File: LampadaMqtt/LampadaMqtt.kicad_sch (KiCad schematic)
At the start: 23 parts, among them Q1 BDW93C, U1 ESP32-C3_SUPERMINI_TH, U2 module_bh1750

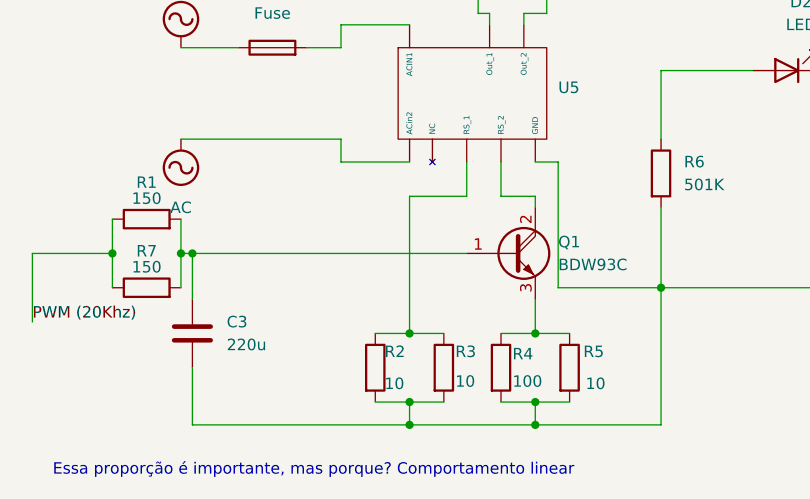
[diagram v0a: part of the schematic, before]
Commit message: Adicionado automations.yaml para refletir automações criadas atualizado esquematica para refletir montagem de fato da lampada e corrigido um erro em mqtt_callback cpp
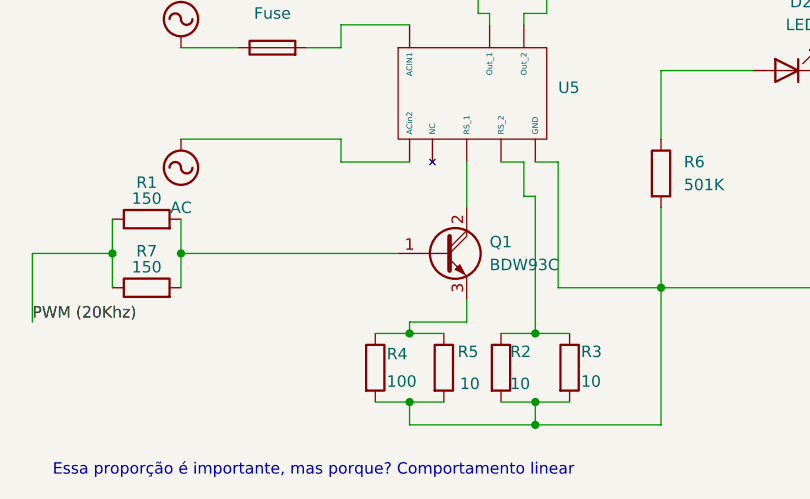
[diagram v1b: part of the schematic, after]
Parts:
- removed C3: 220u, symbol Device:C
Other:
- moved on the sheet: Q1, R2, R3, R4, R5

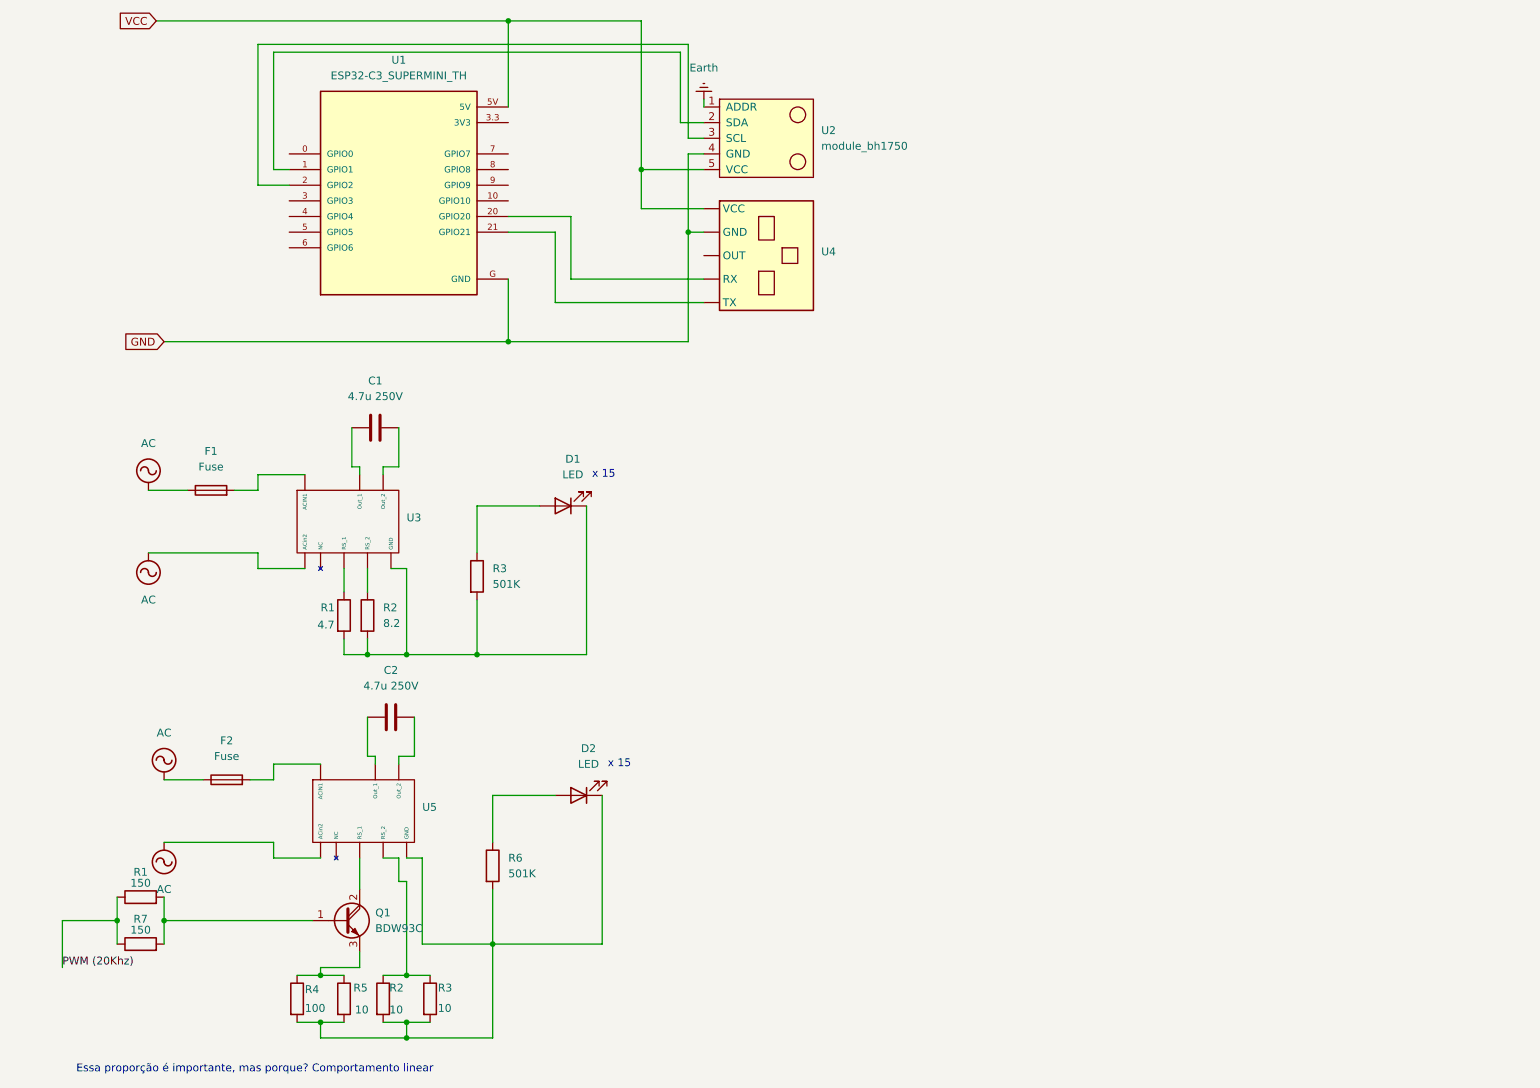
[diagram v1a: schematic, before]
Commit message: Atualização geral para adição de função sleep, relé e controle de brilho
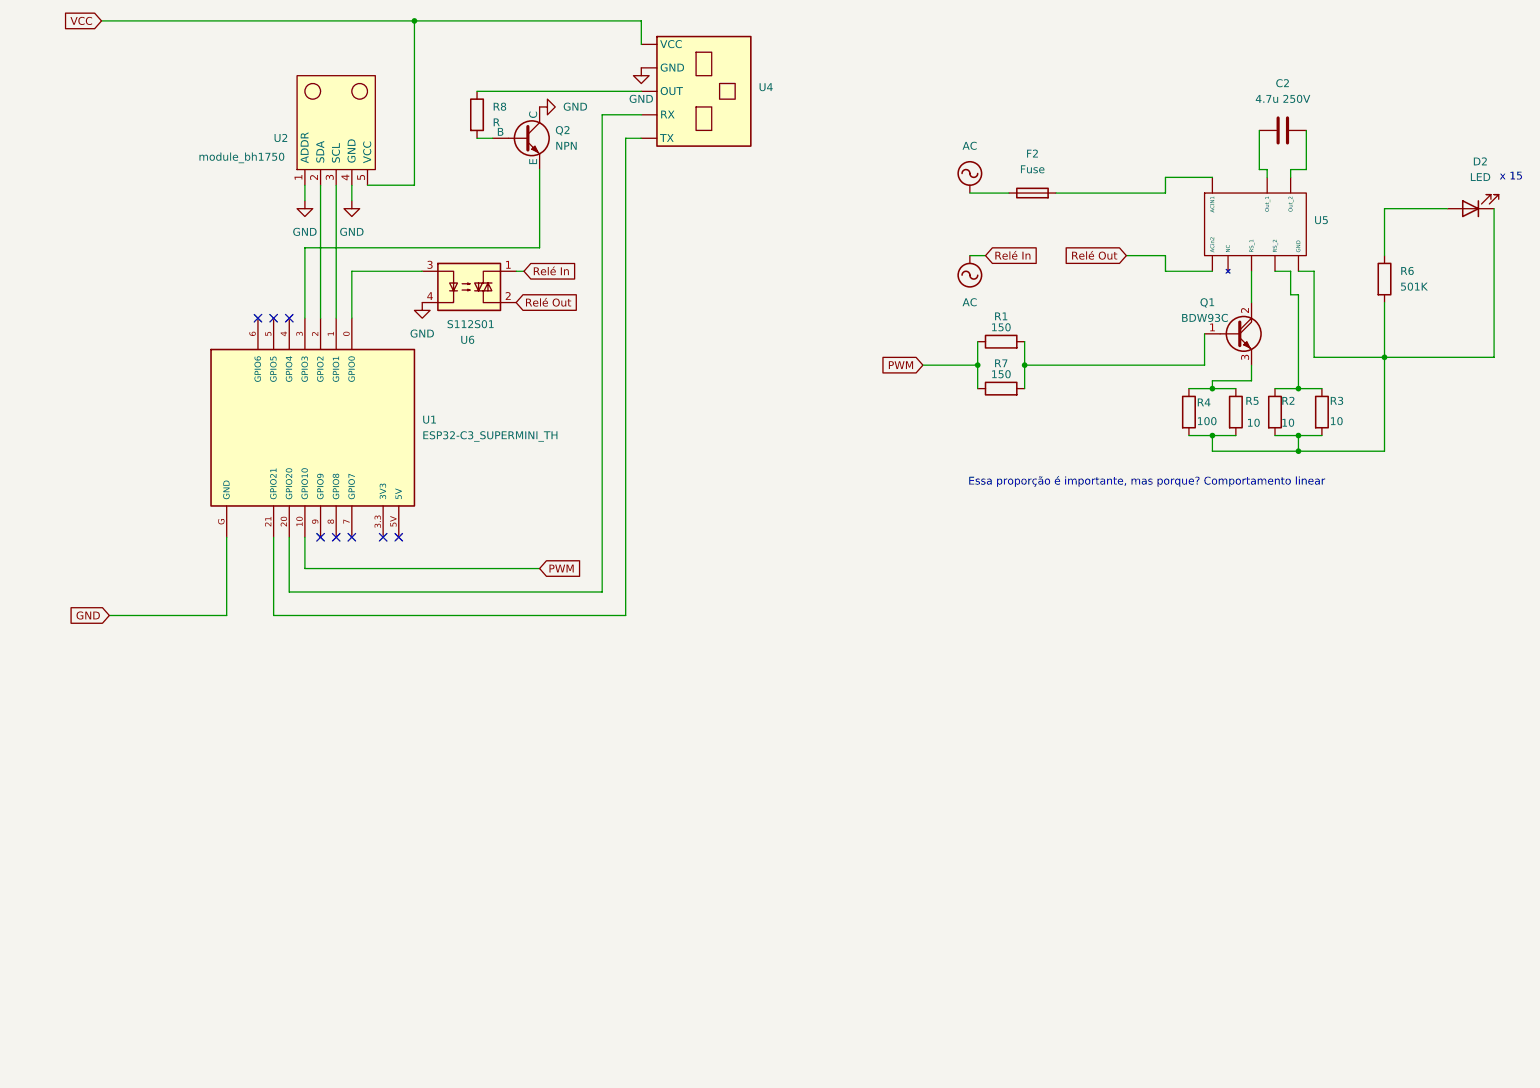
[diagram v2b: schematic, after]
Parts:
- removed C1: 4.7u 250V, symbol Device:C
- removed D1: LED, symbol Device:LED
- removed F1: Fuse, symbol Device:Fuse
- removed R1: 4.7, symbol Device:R
- removed R2: 8.2, symbol Device:R
- removed R3: 501K, symbol Device:R
- removed U3: ~, symbol DIY:JWD1698D
- added Q2: NPN, symbol Simulation_SPICE:NPN
- added R8: R, symbol Device:R
- added U6: S112S01, Package_SIP:SIP4_Sharp-SSR_P7.62mm_Straight, symbol Relay_SolidState:S112S01
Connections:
- net Earth is gone; now on net GND: U2.1 (ADDR)
- net PWM (20Khz) is gone; now on net PWM: R1.1, R7.1
- net AC: now also U6.1; no longer U5. (GND)
- net GND: now also Q2.1 (C), U6.4
- net VCC: no longer U1.5V
- net Relé Out: now reaches U5. (GND)
- net Relé Out: now also U6.2
- net at U2.2 (SDA): now also U1.2 (GPIO2); no longer U1.1 (GPIO1)
- net at U2.3 (SCL): now also U1.1 (GPIO1); no longer U1.2 (GPIO2)
- net at U1.0 (GPIO0): now also U6.3
- net PWM: now reaches U1.10 (GPIO10)
- net at U1.3 (GPIO3): now also Q2.3 (E)
- new net: R8.1, U4. (TX)
- new net: Q2.2 (B), R8.2
- no-connect marks 0 -> 8
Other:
- moved on the sheet: C2, D2, Q1, R1, R2, R3, R4, R5, R6, R7, U1, U2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

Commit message: Adição de sensor de temperatura.
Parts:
- Q2, R8: now not fitted
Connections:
- net VCC: now also U1.5V
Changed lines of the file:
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@@
+	)
+	(no_connect
+		(at 107.95 27.94)
 	)
 	(no_connect
@@
 		(at 66.04 100.33)
 	)
-	(no_connect
-		(at 68.58 100.33)
-	)
 	(wire
 		(pts
@@
 	(wire
 		(pts
+			(xy 68.58 102.87) (xy 66.04 102.87)
+		)
+		(stroke
+			(width 0)
+			(type default)
+		)
+	)
+	(wire
+		(pts
 			(xy 162.56 72.39) (xy 162.56 68.58)
 		)
@@
 		(pts
 			(xy 208.28 34.29) (xy 208.28 40.64)
+		)
+		(stroke
+			(width 0)
+			(type default)
+		)
+	)
+	(wire
+		(pts
+			(xy 68.58 102.87) (xy 68.58 100.33)
 		)
 		(stroke
@@
 				)
 				(justify left)
+				(hide yes)
+			)
+		)
+	)
+	(global_label "VCC"
+		(shape input)
+		(at 66.04 102.87 180)
+		(fields_autoplaced yes)
+		(effects
+			(font
+				(size 1.27 1.27)
+			)
+			(justify right)
+		)
+		(property "Intersheetrefs" "${INTERSHEET_REFS}"
+			(at 59.4262 102.87 0)
+			(effects
+				(font
+					(size 1.27 1.27)
+				)
+				(justify right)
 				(hide yes)
 			)
@@
 		(in_bom yes)
 		(on_board yes)
-		(dnp no)
+		(dnp yes)
 		(fields_autoplaced yes)
 		(property "Reference" "R8"
@@
 		(in_bom yes)
 		(on_board yes)
-		(dnp no)
+		(dnp yes)
 		(fields_autoplaced yes)
 		(property "Reference" "Q2"
@@
 		(on_board yes)
 		(dnp no)
-		(fields_autoplaced yes)
 		(property "Reference" "#PWR06"
 			(at 107.95 30.48 0)
@@
 		)
 		(property "Value" "GND"
-			(at 107.95 29.21 0)
-			(effects
-				(font
+			(at 105.156 24.13 0)
+			(effects
+				(font

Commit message: Atualizado Relatorio
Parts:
- removed Q2: NPN, symbol Simulation_SPICE:NPN
- removed R8: R, symbol Device:R
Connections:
- no-connect marks 8 -> 9
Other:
- note removed: "Essa proporção é importante, mas porque? Comportamento linear"
- title: (none) -> Lâmpada
- moved on the sheet: C2, D2, F2, Q1, R1, R2, R3, R4, R5, R6, R7, U5
